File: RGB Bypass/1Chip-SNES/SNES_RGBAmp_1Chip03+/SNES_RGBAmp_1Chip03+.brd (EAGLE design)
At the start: 28.4 x 18.6 mm, 22 parts

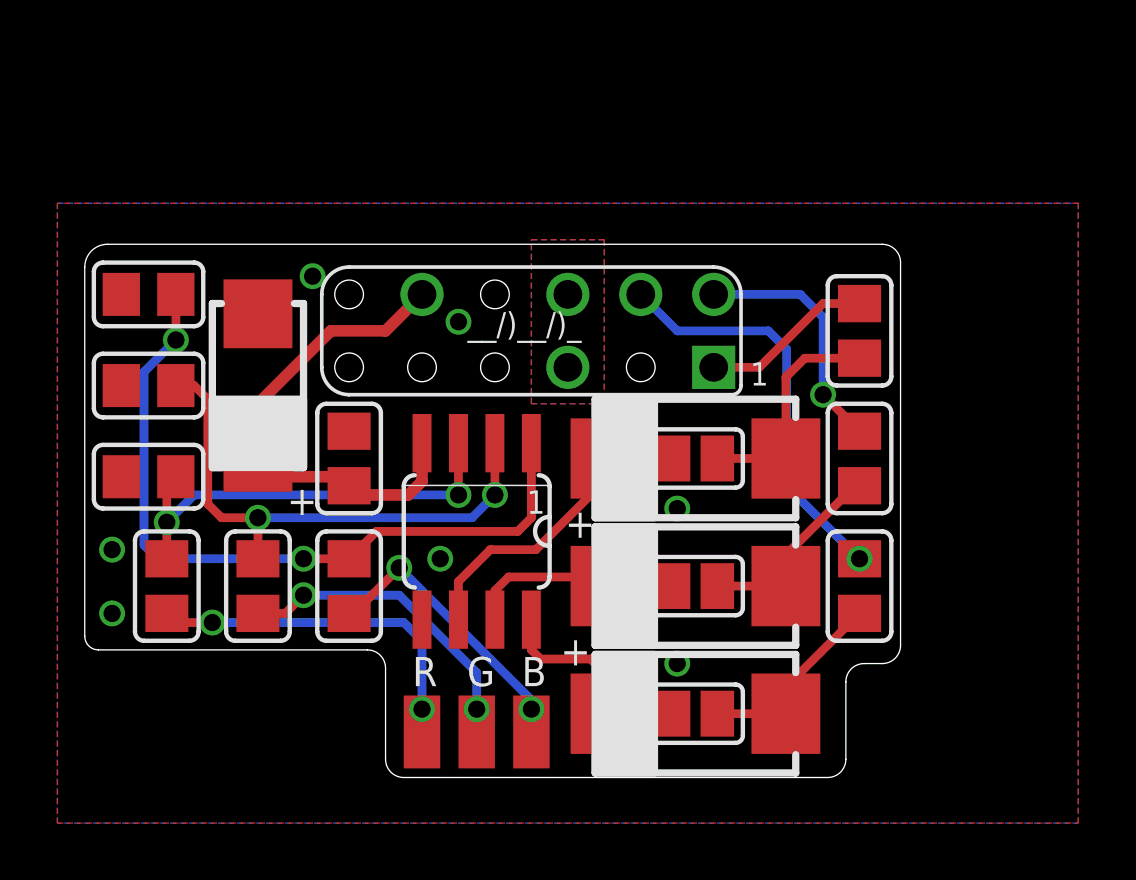
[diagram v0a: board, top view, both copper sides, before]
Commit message: rename folders a bit, add thermals to GND pads
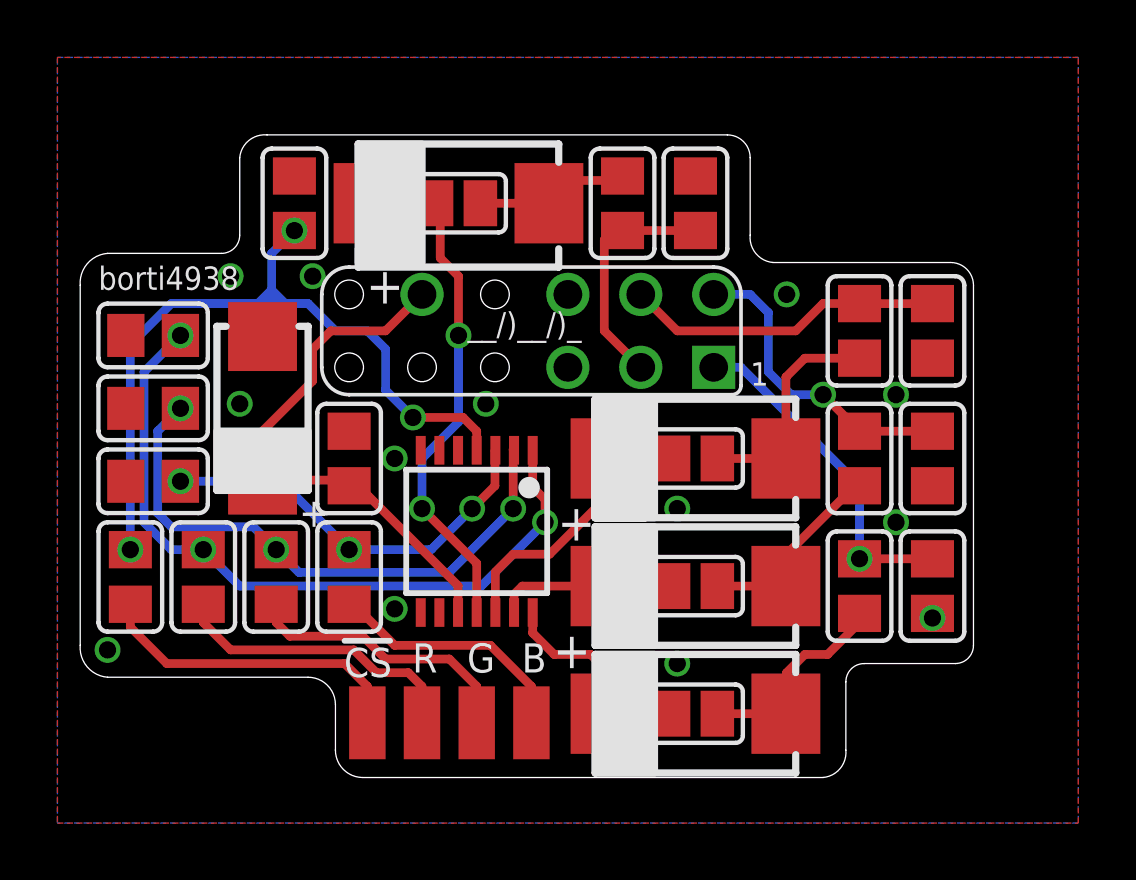
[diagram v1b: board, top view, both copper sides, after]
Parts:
- removed U$1: THS7314, snescart:THS7314
- added C10, C7, C8, C9: 47p, snescart:Z0805
- added C6: 330u, rcl:SMC_D
- added CS: (no value), wirepad:SMD1,27-2,54
- added R10: 75-421, snescart:Z0805
- added R11: 5.0k, snescart:Z0805
- added R12: 4.3k, snescart:Z0805
- added SJ4: (no value), jumper:SJ
- added U$3: SNES_MULTIAV_RGBC_ONLY, snes_div:SNES_MULTIAV_RGBC_ONLY
- U$2: value SNES_MULTIAV_RGB_ONLY -> THS7374; device snes_div:SNES_MULTIAV_RGB_ONLY -> snes_div:THS7374
- moved R1 8.89 mm to (38.1, 29.8)
- moved R3 8.89 mm to (38.1, 38.7)
- moved U$2 7.24 mm to (24.8, 31.8), turned to 180 degrees
- moved R9 6.51 mm to (13.5, 33.5)
- moved R7 4.92 mm to (13.5, 38.6)
- moved R4 1.31 mm to (15.2, 30.2)
- moved C2 0.81 mm to (17.3, 36.0)
- moved R8 0.81 mm to (13.5, 36.0)
- moved R5 0.71 mm to (17.8, 30.2)
- moved R6 0.32 mm to (20.3, 30.2)
- moved B 0.32 mm to (26.7, 25.1)
- moved G 0.32 mm to (24.8, 25.1)
- moved R 0.32 mm to (22.9, 25.1)
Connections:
- removed net N$3: R4.1, R7.2, U$1.3
- new net N$10: R11.1, R12.2, U$2.4
- new net N$17: CS.1, R11.2
- new net N$18: C6.+, SJ4.1, U$2.11
- new net N$19: C6.-, R10.1, SJ4.2
- new net N$20: C10.1, R10.2, U$3.P$3
- new net R9: R6.1, R9.2, U$2.3
- net GND: now also C10.2, C7.2, C8.2, C9.2, R12.1, U$2.5, U$2.6, U$2.9, U$3.P$5, U$3.P$6; no longer U$1.5, U$2.P$5, U$2.P$6
- net N$1: now also R4.1, R7.2, U$2.1; no longer R6.1, R9.2, U$1.1
- net N$11: now also U$2.12; no longer U$1.6
- net N$12: now also U$2.14; no longer U$1.8
- net N$2: now also U$2.2; no longer U$1.2
- net N$4: now also R1.1; no longer R3.1
- net N$5: now also C7.1, R1.2, U$3.P$1; no longer R3.2, U$2.P$4
- net N$6: now also C8.1, U$3.P$2; no longer U$2.P$2
- net N$7: now also U$2.13; no longer U$1.7
- net N$8: now also R3.1; no longer R1.1
- net N$9: now also C9.1, R3.2, U$3.P$4; no longer R1.2, U$2.P$1
- net VCC: now also U$2.10, U$3.P$10; no longer U$1.4, U$2.P$10
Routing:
- net N$10: track 0.00 -> 27.6 mm, vias 0 -> 3
- net N$18: track 0.00 -> 18.3 mm, vias 0 -> 2
- net N$3: track 16.0 -> 0.00 mm, vias 2 -> 0
- net R9: track 0.00 -> 14.8 mm, vias 0 -> 3
- net N$17: track 0.00 -> 11.2 mm
- net N$20: track 0.00 -> 8.22 mm
- net N$19: track 0.00 -> 5.80 mm
- net N$9: track 6.00 -> 11.1 mm
- net VCC: track 17.7 -> 20.5 mm
- net N$14: track 13.1 -> 10.4 mm, vias 2 -> 0
- net N$5: track 14.2 -> 11.9 mm
- net N$6: track 8.64 -> 10.8 mm
- net N$2: track 18.7 -> 20.3 mm, vias 2 -> 3
- net N$7: track 7.56 -> 6.31 mm
- net N$15: track 11.1 -> 9.81 mm, vias 2 -> 0
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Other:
- board size 28.4 x 18.6 mm -> 31.1 x 22.4 mm
- board text added: "(4.3kΩ)"
- board text added: "(5.0kΩ)"
- board text added: "(75Ω- 421Ω)"
- board text added: "C1 (22uF/ 6.3V)"
- board text added: "C10 (47pF)"
- board text added: "C6 (330uF/ 6.3V )"
- board text added: "C7-C9 (47pF) (Jr./Mini only)"
- board text added: "R1-R3 (75Ω, PAL:39Ω)"
- board text added: "R10"
- board text added: "R11"
- board text added: "R12"
- board text added: "RGBAmp for SNES V3.4b"
- board text added: "THS 7374"
- board text added: "borti4938"
- board text removed: "C1 (22uF/ 6.3V )"
- board text removed: "R1-R3 (NTSC:75Ω ,PAL:39Ω)"
- board text removed: "RGBAmp for SNES V3.3"
- board text removed: "THS 7314"
